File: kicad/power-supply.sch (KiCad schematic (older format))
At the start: 24 parts, among them Q2 2N7002, Q3 MMBT3904, Q4 MMBT3904, Q5 ZXMP10A13FTA, SW5 Ein/Aus

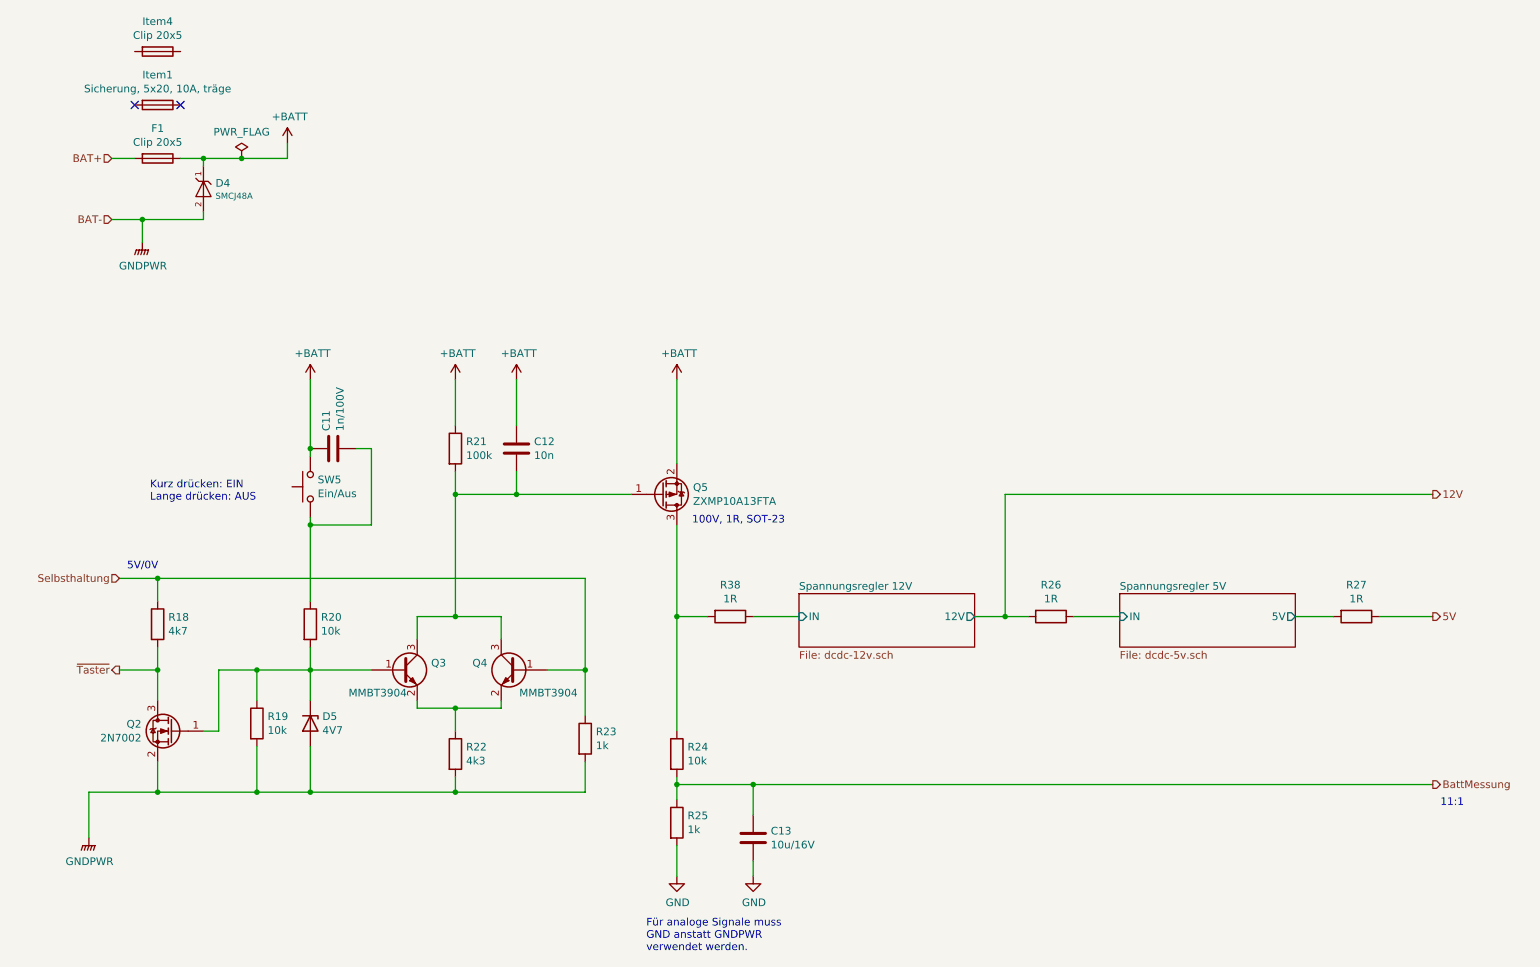
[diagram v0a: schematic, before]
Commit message: BOM ist nun fast fertig
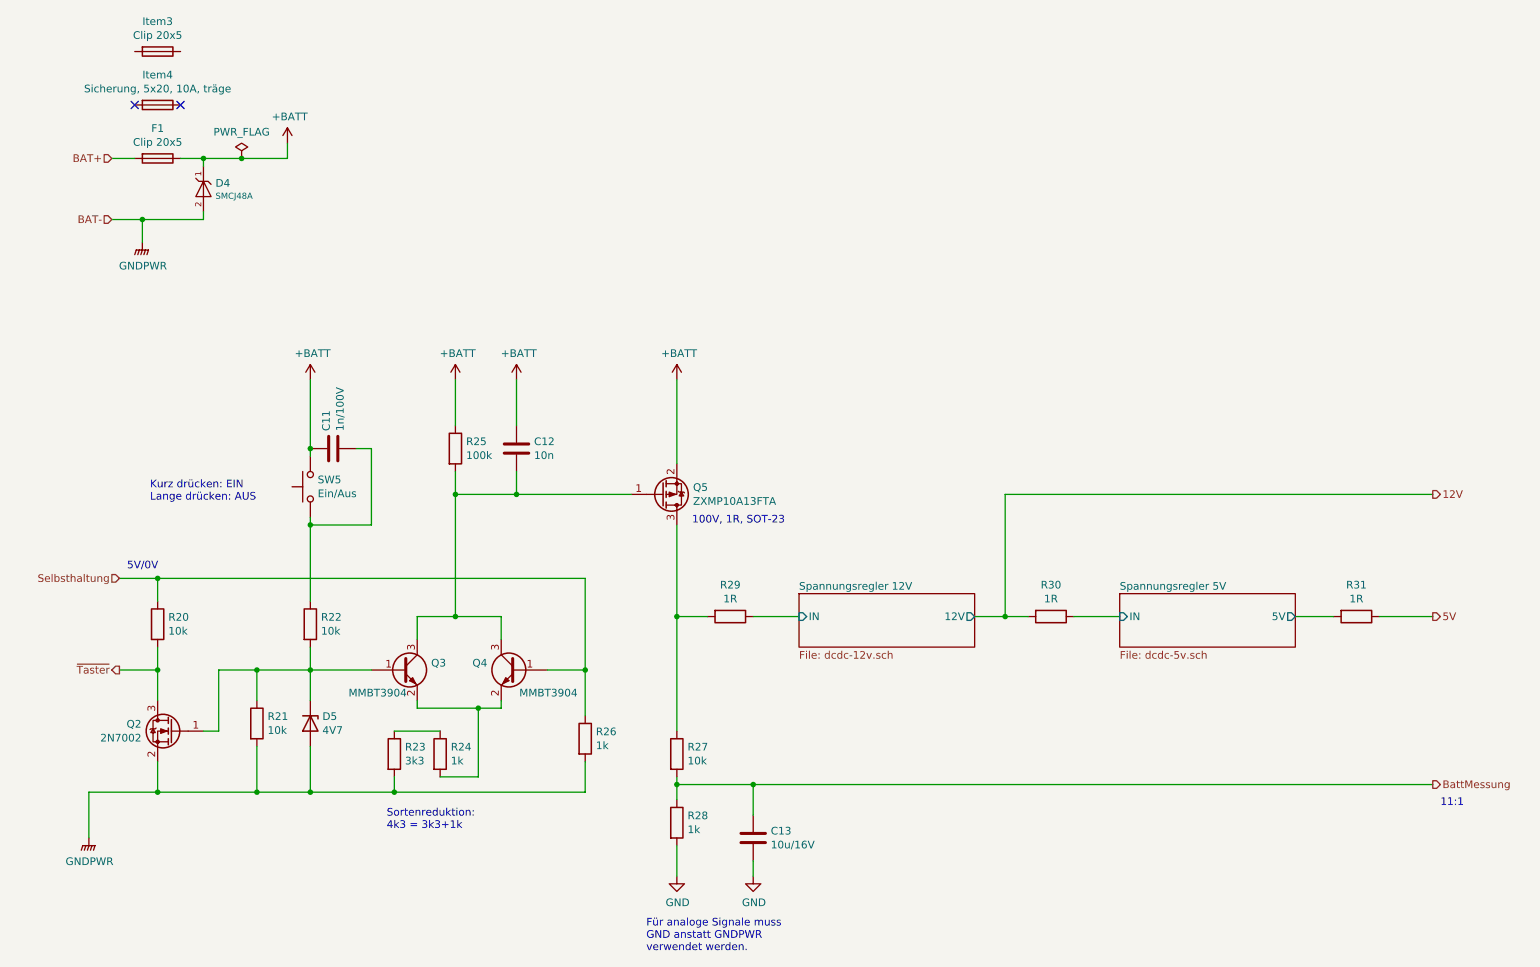
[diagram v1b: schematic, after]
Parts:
- added R24: 1k, Resistor_SMD:R_1206_3216Metric, symbol Device:R
- Q2: ManPartNr (none) -> 2N7002; Manufacturer (none) -> Guangdong Hottech; Notes (none) -> N-Channel 60V 115mA 2.5V @ 250uA 5Ω @ 500mA,10V 225mW SOT-2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; PriceEUR (none) -> 0.0122; PriceForQty (none) -> 50; Weblink (none) -> https://lcsc.com/product-detail/MOSFET_Guangdong-Hottech-2N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
- Q3, Q4: PriceEUR (none) -> 0.0097; PriceForQty (none) -> 50; Weblink (none) -> https://lcsc.com/product-detail/Transistors-NPN-PNP_KEXIN-M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
- Q5: ManPartNr (none) -> ZXMP10A13FTA; Manufacturer (none) -> Diodes; Notes (none) -> P-Channel -100V 600mA 4V @ 250uA 1Ω @ 600mA,10V 625mW SOT-2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; PriceEUR (none) -> 0.2191; PriceForQty (none) -> 100
- R20: renamed from R18; value 4k7 -> 10k; PriceEUR (none) -> 0.01
- R21: renamed from R19; PriceEUR (none) -> 0.01
- R22: renamed from R20; PriceEUR (none) -> 0.01
- R23: renamed from R22; value 4k3 -> 3k3; PriceEUR (none) -> 0.01
- R25: renamed from R21; PriceEUR (none) -> 0.01
- R26: renamed from R23; PriceEUR (none) -> 0.01
- R27: renamed from R24; PriceEUR (none) -> 0.01
- R28: renamed from R25; PriceEUR (none) -> 0.01
- R29: renamed from R38; PriceEUR (none) -> 0.01
- R30: renamed from R26; PriceEUR (none) -> 0.01
- R31: renamed from R27; PriceEUR (none) -> 0.01
- SW5: ManPartNr (none) -> TS-1187A-B-A-B; Manufacturer (none) -> XKB Connectivity; Notes (none) -> SPST 50mA @ 12VDC Vertical Round Button 160gf SMD Tactile S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; PriceEUR (none) -> 0.01; PriceForQty (none) -> 500; Weblink (none) -> https://lcsc.com/product-detail/Tactile-Switches_XKB-Connec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
- renumbered Item4 to Item3, Item1 to Item4
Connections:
- net at Q3.2 (E), Q4.2 (E): now also R24.2; no longer R23.1
- new net: R23.1, R24.1
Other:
- note added: "Sortenreduktion: \n4k3 = 3k3+1k"
- moved on the sheet: R23
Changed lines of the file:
@@
 F 4 "C318884" H 2700 3650 50  0001 C CNN "DistOrderNr"
 F 5 "LCSC" H 2700 3650 50  0001 C CNN "Distributor"
+F 6 "TS-1187A-B-A-B" H 2700 3650 50  0001 C CNN "ManPartNr"
+F 7 "XKB Connectivity" H 2700 3650 50  0001 C CNN "Manufacturer"
+F 8 " 	SPST 50mA @ 12VDC Vertical Round Button 160gf SMD Tactile Switches " H 2700 3650 50  0001 C CNN "Notes"
+F 9 "0.01" H 2700 3650 50  0001 C CNN "PriceEUR"
+F 10 "500" H 2700 3650 50  0001 C CNN "PriceForQty"
+F 11 "https://lcsc.com/product-detail/Tactile-Switches_XKB-Connectivity-TS-1187A-B-A-B_C318884.html" H 2700 3650 50  0001 C CNN "Weblink"
 	1    2700 3650
 	0    -1   -1   0
 $EndComp
 $Comp
-L Device:R R20
+L Device:R R22
 U 1 1 60910786
 P 2700 4550
-F 0 "R20" H 2770 4596 50  0000 L CNN
+F 0 "R22" H 2770 4596 50  0000 L CNN
 F 1 "10k" H 2770 4505 50  0000 L CNN
 F 2 "Resistor_SMD:R_1206_3216Metric" V 2630 4550 50  0001 C CNN
 F 3 "~" H 2700 4550 50  0001 C CNN
+F 4 "0.01" H 2700 4550 50  0001 C CNN "PriceEUR"
 	1    2700 4550
 	1    0    0    -1
 $EndComp
 $Comp
-L Device:R R19
+L Device:R R21
 U 1 1 60910B4F
 P 2350 5200
-F 0 "R19" H 2420 5246 50  0000 L CNN
+F 0 "R21" H 2420 5246 50  0000 L CNN
 F 1 "10k" H 2420 5155 50  0000 L CNN
 F 2 "Resistor_SMD:R_1206_3216Metric" V 2280 5200 50  0001 C CNN
 F 3 "~" H 2350 5200 50  0001 C CNN
+F 4 "0.01" H 2350 5200 50  0001 C CNN "PriceEUR"
 	1    2350 5200
 	1    0    0    -1
@@
 F 4 "C382281" H 3300 4850 50  0001 C CNN "DistOrderNr"
 F 5 "LCSC" H 3300 4850 50  0001 C CNN "Distributor"
+F 6 "0.0097" H 3300 4850 50  0001 C CNN "PriceEUR"
+F 7 "50" H 3300 4850 50  0001 C CNN "PriceForQty"
+F 8 "https://lcsc.com/product-detail/Transistors-NPN-PNP_KEXIN-MMBT3904_C382281.html" H 3300 4850 50  0001 C CNN "Weblink"
 	1    3300 4850
 	1    0    0    -1
@@
 F 4 "C382281" H 4050 4850 50  0001 C CNN "DistOrderNr"
 F 5 "LCSC" H 4050 4850 50  0001 C CNN "Distributor"
+F 6 "0.0097" H 4050 4850 50  0001 C CNN "PriceEUR"
+F 7 "50" H 4050 4850 50  0001 C CNN "PriceForQty"
+F 8 "https://lcsc.com/product-detail/Transistors-NPN-PNP_KEXIN-MMBT3904_C382281.html" H 4050 4850 50  0001 C CNN "Weblink"
 	1    4050 4850
 	-1   0    0    -1
 $EndComp
 $Comp
-L Device:R R21
+L Device:R R25
 U 1 1 60918ACF
 P 3650 3400
-F 0 "R21" H 3720 3446 50  0000 L CNN
+F 0 "R25" H 3720 3446 50  0000 L CNN
 F 1 "100k" H 3720 3355 50  0000 L CNN
 F 2 "Resistor_SMD:R_1206_3216Metric" V 3580 3400 50  0001 C CNN
 F 3 "~" H 3650 3400 50  0001 C CNN
+F 4 "0.01" H 3650 3400 50  0001 C CNN "PriceEUR"
 	1    3650 3400
 	1    0    0    -1
@@
 	3650 3700 3650 3550
 $Comp
-L Device:R R22
+L Device:R R23
 U 1 1 6091D735
-P 3650 5400
-F 0 "R22" H 3720 5446 50  0000 L CNN
-F 1 "4k3" H 3720 5355 50  0000 L CNN
-F 2 "Resistor_SMD:R_1206_3216Metric" V 3580 5400 50  0001 C CNN
-F 3 "~" H 3650 5400 50  0001 C CNN
-	1    3650 5400
+P 3250 5400
+F 0 "R23" H 3320 5446 50  0000 L CNN
+F 1 "3k3" H 3320 5355 50  0000 L CNN
+F 2 "Resistor_SMD:R_1206_3216Metric" V 3180 5400 50  0001 C CNN
+F 3 "~" H 3250 5400 50  0001 C CNN
+F 4 "0.01" H 3250 5400 50  0001 C CNN "PriceEUR"
+	1    3250 5400
 	1    0    0    -1
 $EndComp
@@
 	3400 5050 3400 5100
 Wire Wire Line
-	3400 5100 3650 5100
-Wire Wire Line
 	3950 5100 3950 5050
 Wire Wire Line
-	3650 5100 3650 5250
-Connection ~ 3650 5100
-Wire Wire Line
-	3650 5100 3950 5100
-Wire Wire Line
-	3650 5550 3650 5650
+	3250 5550 3250 5650
 Text HLabel 1450 4250 0    50   Input ~ 0
 Selbsthaltung
@@
 5V/0V
 $Comp
-L Device:R R23
+L Device:R R26
 U 1 1 6095473F
 P 4500 5300
-F 0 "R23" H 4570 5346 50  0000 L CNN
+F 0 "R26" H 4570 5346 50  0000 L CNN
 F 1 "1k" H 4570 5255 50  0000 L CNN
 F 2 "Resistor_SMD:R_1206_3216Metric" V 4430 5300 50  0001 C CNN
 F 3 "~" H 4500 5300 50  0001 C CNN
+F 4 "0.01" H 4500 5300 50  0001 C CNN "PriceEUR"
 	1    4500 5300
 	1    0    0    -1
@@
 	2000 1850 2000 1900
 $Comp
-L Device:Fuse Item1
+L Device:Fuse Item4
 U 1 1 60965E2A
 P 1700 1150
-F 0 "Item1" V 1503 1150 50  0000 C CNN
+F 0 "Item4" V 1503 1150 50  0000 C CNN
 F 1 "Sicherung, 5x20, 10A, träge" V 1594 1150 50  0000 C CNN
 F 2 "htl_virtual:Virtual-Item" V 1630 1150 50  0001 C CNN
@@
 F 4 "C50185" H 5000 3700 50  0001 C CNN "DistOrderNr"
 F 5 "LCSC" H 5000 3700 50  0001 C CNN "Distributor"
+F 6 "ZXMP10A13FTA" H 5000 3700 50  0001 C CNN "ManPartNr"
+F 7 "Diodes" H 5000 3700 50  0001 C CNN "Manufacturer"
+F 8 "P-Channel -100V 600mA 4V @ 250uA 1Ω @ 600mA,10V 625mW SOT-23(SOT-23-3) MOSFET" H 5000 3700 50  0001 C CNN "Notes"
+F 9 "0.2191" H 5000 3700 50  0001 C CNN "PriceEUR"
+F 10 "100" H 5000 3700 50  0001 C CNN "PriceForQty"
 	1    5000 3700
 	1    0    0    1
@@
 F 4 "C181082" H 1800 5250 50  0001 C CNN "DistOrderNr"
 F 5 "LCSC" H 1800 5250 50  0001 C CNN "Distributor"
+F 6 "2N7002" H 1800 5250 50  0001 C CNN "ManPartNr"
+F 7 "Guangdong Hottech" H 1800 5250 50  0001 C CNN "Manufacturer"
+F 8 "N-Channel 60V 115mA 2.5V @ 250uA 5Ω @ 500mA,10V 225mW SOT-23(SOT-23-3) MOSFET" H 1800 5250 50  0001 C CNN "Notes"
+F 9 "0.0122" H 1800 5250 50  0001 C CNN "PriceEUR"
+F 10 "50" H 1800 5250 50  0001 C CNN "PriceForQty"
+F 11 "https://lcsc.com/product-detail/MOSFET_Guangdong-Hottech-2N7002_C181082.html" H 1800 5250 50  0001 C CNN "Weblink"
 	1    1800 5250
 	-1   0    0    -1
@@
 Connection ~ 2700 5650
 Wire Wire Line
-	2700 5650 3650 5650
-Connection ~ 3650 5650
-Wire Wire Line
-	3650 5650 4500 5650
+	2700 5650 3250 5650
+Connection ~ 3250 5650
+Wire Wire Line
+	3250 5650 4500 5650
 Wire Wire Line
 	9150 4500 9400 4500
@@
 	7050 4500 7250 4500
 $Comp
-L Device:R R26
+L Device:R R30
 U 1 1 60A621EF
 P 7550 4500
-F 0 "R26" V 7343 4500 50  0000 C CNN
+F 0 "R30" V 7343 4500 50  0000 C CNN
 F 1 "1R" V 7434 4500 50  0000 C CNN
 F 2 "Resistor_SMD:R_1206_3216Metric" V 7480 4500 50  0001 C CNN
 F 3 "~" H 7550 4500 50  0001 C CNN
+F 4 "0.01" H 7550 4500 50  0001 C CNN "PriceEUR"
 	1    7550 4500
 	0    1    1    0
 $EndComp
 $Comp
-L Device:R R27
+L Device:R R31
 U 1 1 60A6EE4B
 P 9550 4500
-F 0 "R27" V 9343 4500 50  0000 C CNN
+F 0 "R31" V 9343 4500 50  0000 C CNN
 F 1 "1R" V 9434 4500 50  0000 C CNN
 F 2 "Resistor_SMD:R_1206_3216Metric" V 9480 4500 50  0001 C CNN
 F 3 "~" H 9550 4500 50  0001 C CNN
+F 4 "0.01" H 9550 4500 50  0001 C CNN "PriceEUR"
 	1    9550 4500
 	0    1    1    0
@@
 	7250 4500 7400 4500
 $Comp
-L Device:R R24
+L Device:R R27
 U 1 1 60A7F224
 P 5100 5400
-F 0 "R24" H 5170 5446 50  0000 L CNN
+F 0 "R27" H 5170 5446 50  0000 L CNN
 F 1 "10k" H 5170 5355 50  0000 L CNN
 F 2 "Resistor_SMD:R_1206_3216Metric" V 5030 5400 50  0001 C CNN
 F 3 "~" H 5100 5400 50  0001 C CNN
+F 4 "0.01" H 5100 5400 50  0001 C CNN "PriceEUR"
 	1    5100 5400
 	1    0    0    -1
 $EndComp
 $Comp
-L Device:R R25
+L Device:R R28
 U 1 1 60A7F6D0
 P 5100 5850
-F 0 "R25" H 5170 5896 50  0000 L CNN
+F 0 "R28" H 5170 5896 50  0000 L CNN
 F 1 "1k" H 5170 5805 50  0000 L CNN
 F 2 "Resistor_SMD:R_1206_3216Metric" V 5030 5850 50  0001 C CNN
 F 3 "~" H 5100 5850 50  0001 C CNN
+F 4 "0.01" H 5100 5850 50  0001 C CNN "PriceEUR"
 	1    5100 5850
 	1    0    0    -1
@@
 Für analoge Signale muss\nGND anstatt GNDPWR \nverwendet werden.
 $Comp
-L Device:R R18
+L Device:R R20
 U 1 1 60AD33A8
 P 1700 4550
-F 0 "R18" H 1770 4596 50  0000 L CNN
-F 1 "4k7" H 1770 4505 50  0000 L CNN
+F 0 "R20" H 1770 4596 50  0000 L CNN
+F 1 "10k" H 1770 4505 50  0000 L CNN
 F 2 "Resistor_SMD:R_1206_3216Metric" V 1630 4550 50  0001 C CNN
 F 3 "~" H 1700 4550 50  0001 C CNN
+F 4 "0.01" H 1700 4550 50  0001 C CNN "PriceEUR"
 	1    1700 4550
 	1    0    0    -1
@@
 Connection ~ 5100 4500
 $Comp
-L Device:R R38
+L Device:R R29
 U 1 1 60B60B7F
 P 5450 4500
-F 0 "R38" V 5243 4500 50  0000 C CNN
+F 0 "R29" V 5243 4500 50  0000 C CNN
 F 1 "1R" V 5334 4500 50  0000 C CNN
 F 2 "Resistor_SMD:R_1206_3216Metric" V 5380 4500 50  0001 C CNN
 F 3 "~" H 5450 4500 50  0001 C CNN
+F 4 "0.01" H 5450 4500 50  0001 C CNN "PriceEUR"
 	1    5450 4500
 	0    1    1    0
@@
 	5600 4500 5900 4500
 $Comp
-L Device:Fuse Item4
+L Device:Fuse Item3
 U 1 1 60B6160E
 P 1700 800
-F 0 "Item4" V 1503 800 50  0000 C CNN
+F 0 "Item3" V 1503 800 50  0000 C CNN
 F 1 "Clip 20x5" V 1594 800 50  0000 C CNN
 F 2 "htl_virtual:Virtual-Item" V 1630 800 50  0001 C CNN
@@
 	0    1    1    0
 $EndComp
+Wire Wire Line
+	3400 5100 3800 5100
+$Comp
+L Device:R R24
+U 1 1 60909916
+P 3550 5400
+F 0 "R24" H 3620 5446 50  0000 L CNN
+F 1 "1k" H 3620 5355 50  0000 L CNN
+F 2 "Resistor_SMD:R_1206_3216Metric" V 3480 5400 50  0001 C CNN
+F 3 "~" H 3550 5400 50  0001 C CNN
+F 4 "0.01" H 3550 5400 50  0001 C CNN "PriceEUR"
+	1    3550 5400
+	1    0    0    -1
+$EndComp
+Wire Wire Line
+	3250 5250 3550 5250
+Wire Wire Line
+	3800 5550 3800 5100
+Wire Wire Line
+	3550 5550 3800 5550
+Connection ~ 3800 5100
+Wire Wire Line
+	3800 5100 3950 5100
+Text Notes 3200 5900 0    50   ~ 0
+Sortenreduktion: \n4k3 = 3k3+1k
 $EndSCHEMATC

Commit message: BOM Fertig, 3D auch fast fertig. Ein paar Footrpints fehlen noch.
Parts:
- Item3, Item4: symbol Device:Fuse -> htl_virtual:Item
- R32: renamed from R20; DistOrderNr (none) -> C118075; Distributor (none) -> LCSC
- R33: renamed from R21; DistOrderNr (none) -> C118075; Distributor (none) -> LCSC
- R34: renamed from R22; DistOrderNr (none) -> C118075; Distributor (none) -> LCSC
- R35: renamed from R23; DistOrderNr (none) -> C229599; Distributor (none) -> LCSC
- R36: renamed from R24; DistOrderNr (none) -> C104601; Distributor (none) -> LCSC; ManPartNr (none) -> RTT03101JTP; Manufacturer (none) -> RALEC; Notes (none) -> 1kΩ ±5% 0.25W ±100ppm/℃ 1206 Chip Resistor; PriceEUR 0.01 -> 0.0042; PriceForQty (none) -> 50
- R37: renamed from R25; DistOrderNr (none) -> C269765; Distributor (none) -> LCSC
- R38: renamed from R26; DistOrderNr (none) -> C104601; Distributor (none) -> LCSC; ManPartNr (none) -> RTT03101JTP; Manufacturer (none) -> RALEC; Notes (none) -> 1kΩ ±5% 0.25W ±100ppm/℃ 1206 Chip Resistor; PriceEUR 0.01 -> 0.0042; PriceForQty (none) -> 50
- R39: renamed from R27; DistOrderNr (none) -> C118075; Distributor (none) -> LCSC
- R40: renamed from R28; DistOrderNr (none) -> C104601; Distributor (none) -> LCSC; ManPartNr (none) -> RTT03101JTP; Manufacturer (none) -> RALEC; Notes (none) -> 1kΩ ±5% 0.25W ±100ppm/℃ 1206 Chip Resistor; PriceEUR 0.01 -> 0.0042; PriceForQty (none) -> 50
- R41: renamed from R29; DistOrderNr (none) -> C17928; Distributor (none) -> LCSC
- R42: renamed from R30; DistOrderNr (none) -> C17928; Distributor (none) -> LCSC
- R43: renamed from R31; DistOrderNr (none) -> C17928; Distributor (none) -> LCSC
- SW6: renamed from SW5; Notes SPST 50mA @ 12VDC Vertical Round Button 160gf SMD Tactile Switches -> SPST 50mA @ 12VDC Vertical Round Button 160gf SMD Tactile Switches
- renumbered C11 to C22, C12 to C23, C13 to C24, D4 to D8, D5 to D9
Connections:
- no-connect marks 2 -> 0

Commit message: kleinere Updates im Schaltplan
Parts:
- R37: value 100k -> 10k; DistOrderNr C269765 -> C118075
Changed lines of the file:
@@
 P 3650 3400
 F 0 "R37" H 3720 3446 50  0000 L CNN
-F 1 "100k" H 3720 3355 50  0000 L CNN
+F 1 "10k" H 3720 3355 50  0000 L CNN
 F 2 "Resistor_SMD:R_1206_3216Metric" V 3580 3400 50  0001 C CNN
 F 3 "~" H 3650 3400 50  0001 C CNN
 F 4 "0.01" H 3650 3400 50  0001 C CNN "PriceEUR"
-F 5 "C269765" H 3650 3400 50  0001 C CNN "DistOrderNr"
+F 5 "C118075" H 3650 3400 50  0001 C CNN "DistOrderNr"
 F 6 "LCSC" H 3650 3400 50  0001 C CNN "Distributor"
 	1    3650 3400

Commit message: Bestellte Version v21.0.0
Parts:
- added X4: GND-Öse, htl_smd:Keystone_5016, symbol Connector_Generic:Conn_01x01
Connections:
- net GND: now also X4.1 (Pin_1)
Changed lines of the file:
@@
 encoding utf-8
 Sheet 6 10
-Title "JBC-Miniregler"
-Date "2021-05-02"
-Rev "0.0.1"
+Title "HTL Lötregler Mini"
+Date "2021-06-01"
+Rev "21.0.0"
 Comp "HTL Steyr"
-Comment1 "Prof. Karl Zeilhofer"
+Comment1 "Prof. Karl Zeilhofer et al."
 Comment2 ""
 Comment3 ""
@@
 Wire Wire Line
 	9900 3700 10050 3700
+$Comp
+L power:GND #PWR063
+U 1 1 60B7CAD7
+P 6450 6200
+F 0 "#PWR063" H 6450 5950 50  0001 C CNN
+F 1 "GND" H 6455 6027 50  0000 C CNN
+F 2 "" H 6450 6200 50  0001 C CNN
+F 3 "" H 6450 6200 50  0001 C CNN
+	1    6450 6200
+	1    0    0    -1
+$EndComp
+$Comp
+L Connector_Generic:Conn_01x01 X4
+U 1 1 60B7EA5B
+P 6650 6050
+F 0 "X4" H 6730 6092 50  0000 L CNN
+F 1 "GND-Öse" H 6730 6001 50  0000 L CNN
+F 2 "htl_smd:Keystone_5016" H 6650 6050 50  0001 C CNN
+F 3 "~" H 6650 6050 50  0001 C CNN
+	1    6650 6050
+	1    0    0    -1
+$EndComp
+Wire Wire Line
+	6450 6050 6450 6200
 $EndSCHEMATC
